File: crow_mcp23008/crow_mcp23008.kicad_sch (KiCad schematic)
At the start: 22 parts, among them J1 Conn_02x03_Odd_Even, J2 MJ-3523-SMT-TR, J3 MJ-3523-SMT-TR, J4 MJ-3523-SMT-TR, J5 MJ-3523-SMT-TR, J6 MJ-3523-SMT-TR, J7 MJ-3523-SMT-TR, J8 MJ-3523-SMT-TR, J9 Conn_02x05_Odd_Even, U1 MCP23008-xP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

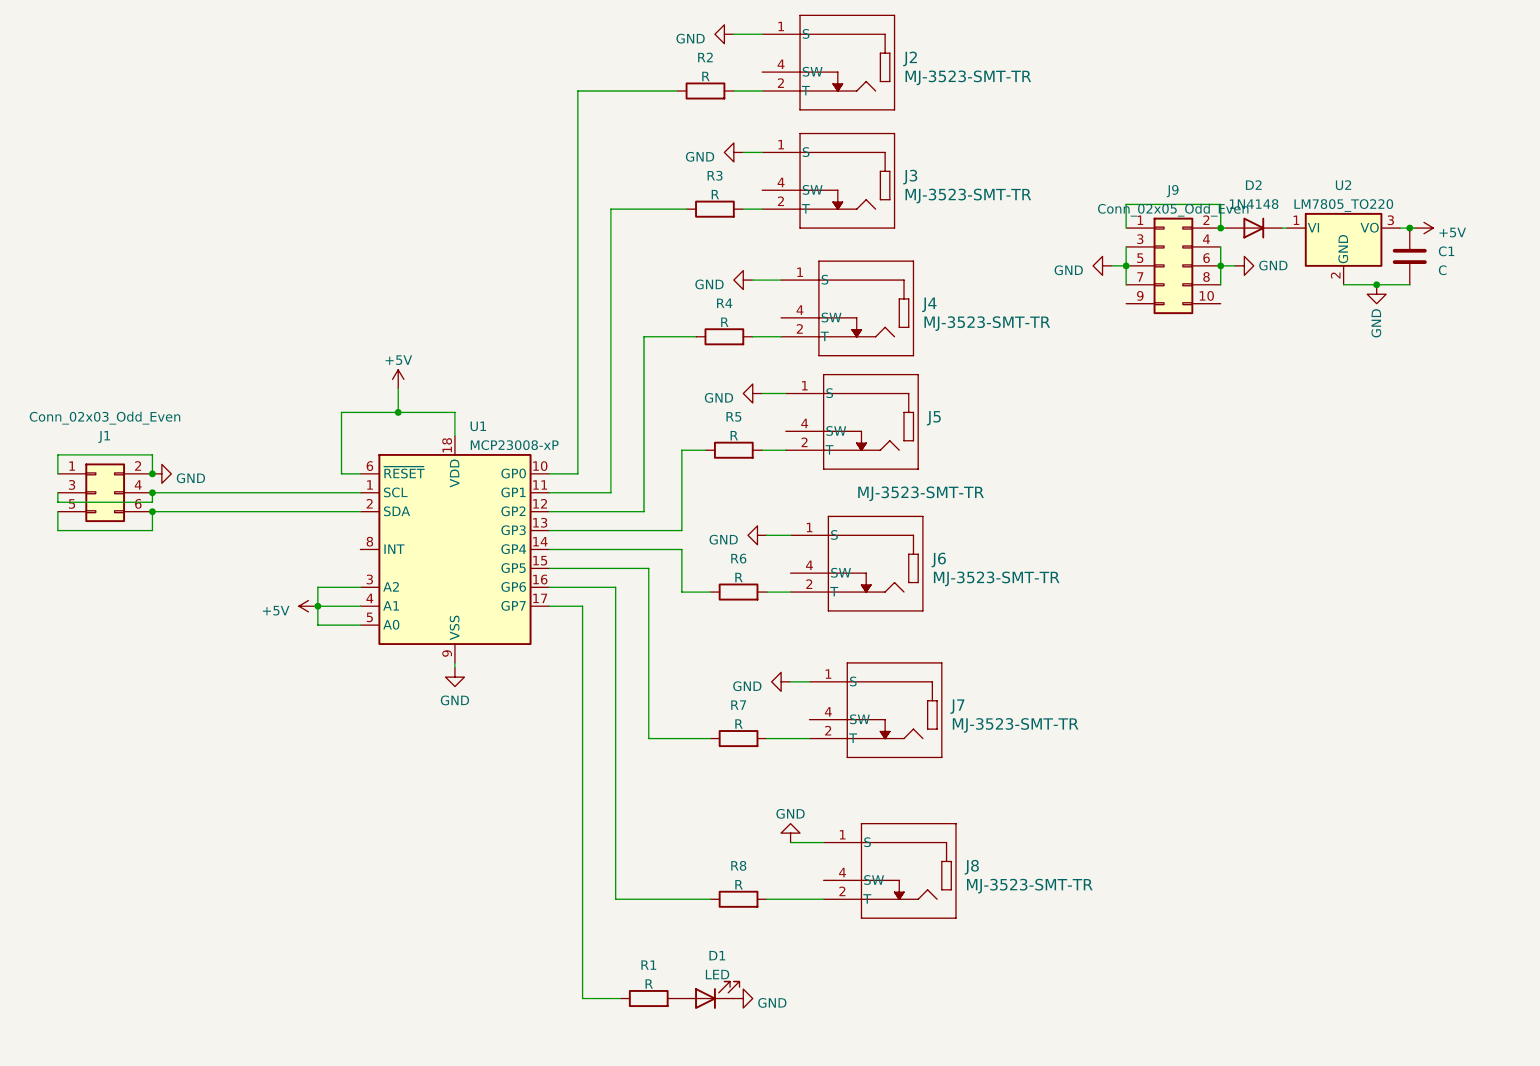
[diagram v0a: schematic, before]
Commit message: v1.1
all SMT w/ LED's
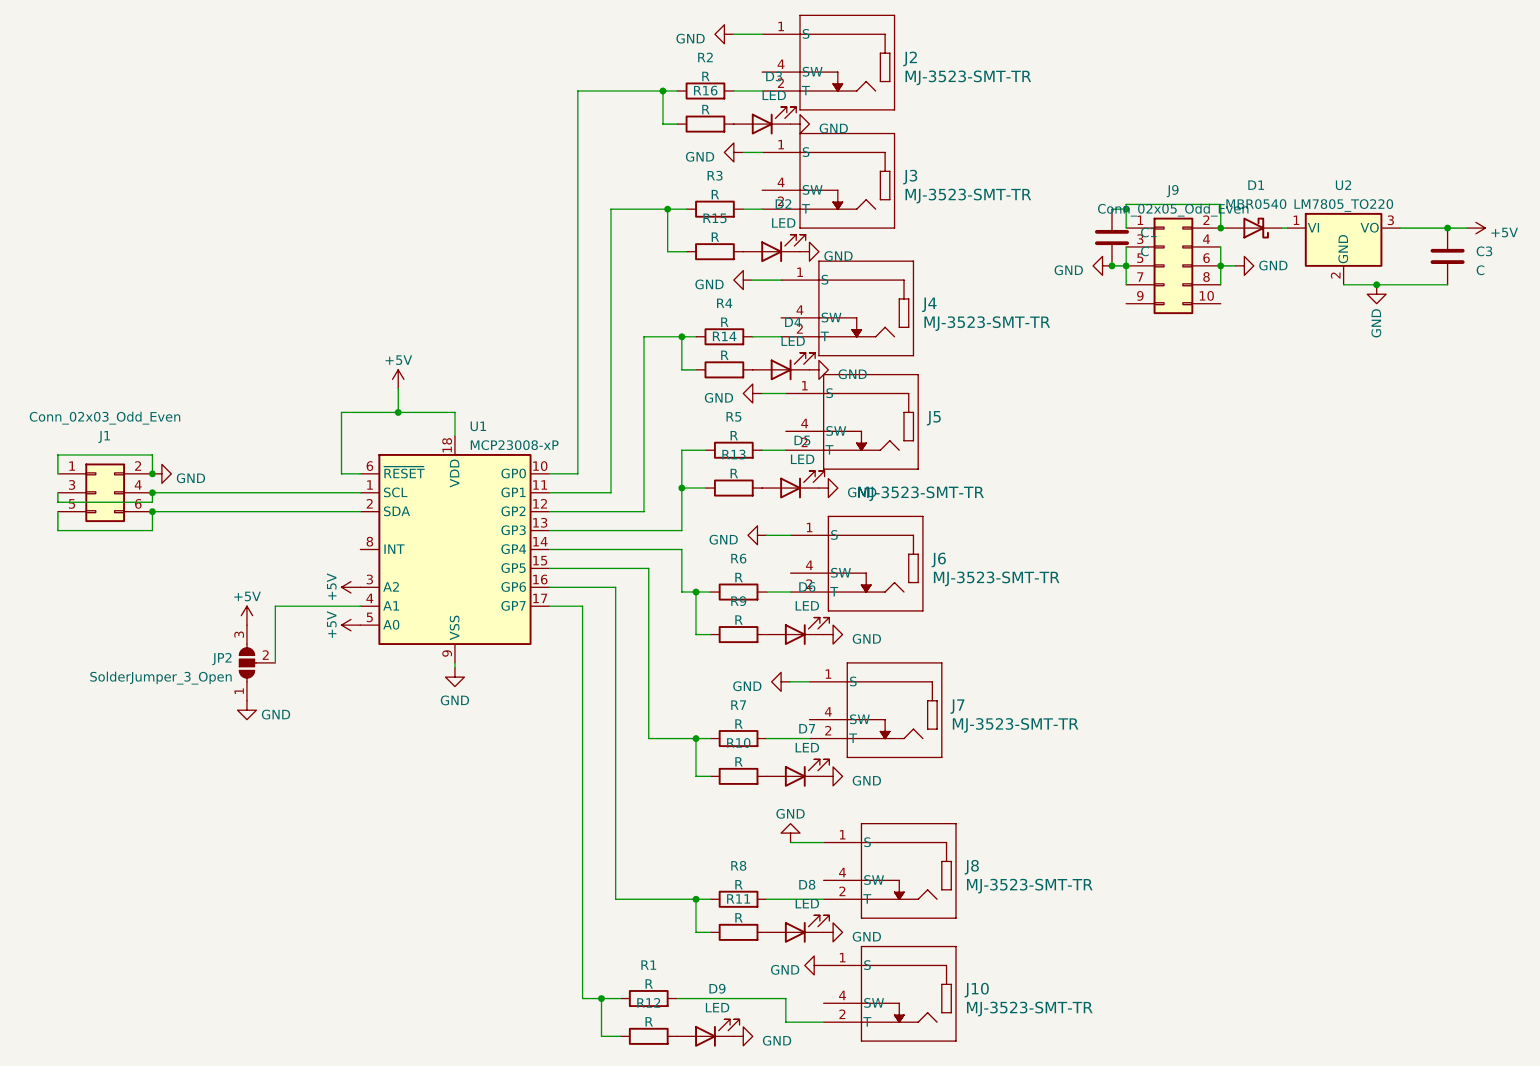
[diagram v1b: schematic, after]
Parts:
- removed D1: LED, LED_THT:LED_D3.0mm_FlatTop, symbol Device:LED
- removed D2: 1N4148, Diode_THT:D_DO-35_SOD27_P7.62mm_Horizontal, symbol Diode:1N4148
- added C3: C, Capacitor_SMD:C_1206_3216Metric_Pad1.33x1.80mm_HandSolder, symbol Device:C
- added D1: MBR0540, Diode_SMD:D_SOD-123, symbol Diode:MBR0540
- added D2, D3, D4, D5, D6, D7, D8, D9: LED, LED_SMD:LED_1206_3216Metric_Pad1.42x1.75mm_HandSolder, symbol Device:LED
- added J10: MJ-3523-SMT-TR, Connector_Audio:CONN_MJ-3523_CUD, symbol Audio:MJ-3523-SMT-TR
- added JP2: SolderJumper_3_Open, Jumper:SolderJumper-3_P2.0mm_Open_TrianglePad1.0x1.5mm_NumberLabels, symbol Jumper:SolderJumper_3_Open
- added R10, R11, R12, R13, R14, R15, R16, R9: R, Resistor_SMD:R_1206_3216Metric_Pad1.30x1.75mm_HandSolder, symbol Device:R
- C1: footprint Capacitor_THT:C_Disc_D5.0mm_W2.5mm_P2.50mm -> Capacitor_SMD:C_1206_3216Metric_Pad1.33x1.80mm_HandSolder
- R1, R2, R3, R4, R5, R6, R7, R8: footprint Resistor_THT:R_Axial_DIN0207_L6.3mm_D2.5mm_P7.62mm_Horizontal -> Resistor_SMD:R_1206_3216Metric_Pad1.30x1.75mm_HandSolder
- U1: footprint Package_DIP:DIP-18_W7.62mm_Socket_LongPads -> Package_SO:SOIC-18W_7.5x11.6mm_P1.27mm
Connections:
- net +5V: now also C3.1, JP2.3 (B); no longer C1.1, U1.4 (A1)
- net GND: now also C3.2, D2.1 (K), D3.1 (K), D4.1 (K), D5.1 (K), D6.1 (K), D7.1 (K), D8.1 (K), D9.1 (K), J10.1 (S), JP2.1 (A)
- net at U2.1 (VI): now also D1.1 (K)
- net at J9.1 (Pin_1), J9.2 (Pin_2): now also C1.1, D1.2 (A)
- net at R5.1, U1.13 (GP3): now also R13.1
- net at R6.1, U1.14 (GP4): now also R9.1
- net at R4.1, U1.12 (GP2): now also R14.1
- net at R3.1, U1.11 (GP1): now also R15.1
- net at R8.1, U1.16 (GP6): now also R11.1
- net at R1.1, U1.17 (GP7): now also R12.1
- net at R1.2: now also J10.2 (T)
- net at R2.1, U1.10 (GP0): now also R16.1
- net at R7.1, U1.15 (GP5): now also R10.1
- new net: D9.2 (A), R12.2
- new net: D2.2 (A), R15.2
- new net: D3.2 (A), R16.2
- new net: D4.2 (A), R14.2
- new net: JP2.2 (C), U1.4 (A1)
- new net: D7.2 (A), R10.2
- new net: D5.2 (A), R13.2
- new net: D8.2 (A), R11.2
- new net: D6.2 (A), R9.2
